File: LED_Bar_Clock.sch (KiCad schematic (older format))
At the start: 51 parts

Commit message: use core libraries for type c connector symbol
Some files seem to have changed format due to the change between
5.0.0 and 5.1.0 of KiCad. This is reflected in this commit
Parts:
- J?: symbol LED_Bar_Clock-rescue:USB_C_Receptacle_USB2.0-Connector -> Connector:USB_C_Receptacle_USB2.0
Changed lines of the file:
@@
 EESchema Schematic File Version 4
 LIBS:LED_Bar_Clock-cache
-EELAYER 26 0
+EELAYER 29 0
 EELAYER END
 $Descr A4 11693 8268
@@
 $EndComp
 $Comp
-L LED_Bar_Clock-rescue:USB_C_Receptacle_USB2.0-Connector J?
+L Connector:USB_C_Receptacle_USB2.0 J?
 U 1 1 5BF122DB
 P 3900 1150

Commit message: add annotations and power flags
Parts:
- gave numbers to parts that had none: 51
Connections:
- no-connect marks 2 -> 4

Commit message: change reset switch in schematic
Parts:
- removed SW1: SW_SPST, symbol Switch:SW_SPST
- added SW1: SKHMQKE010, Clock_Footprints:SKHMQKE010, symbol Clock_Symbols:SKHMQKE010
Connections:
- wire segments 191 -> 203
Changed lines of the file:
@@
 	3900 1950 4000 1950
-$Comp
-L Switch:SW_SPST SW1
-U 1 1 5CC780C2
-P 3850 4750
-F 0 "SW1" V 3804 4848 50  0000 L CNN
-F 1 "SW_SPST" V 3895 4848 50  0000 L CNN
-F 2 "" H 3850 4750 50  0001 C CNN
-F 3 "" H 3850 4750 50  0001 C CNN
-	1    3850 4750
-	0    1    1    0
-$EndComp
-$Comp
-L power:GND #PWR0120
-U 1 1 5CC781C6
-P 3850 5000
-F 0 "#PWR0120" H 3850 4750 50  0001 C CNN
-F 1 "GND" H 3855 4827 50  0000 C CNN
-F 2 "" H 3850 5000 50  0001 C CNN
-F 3 "" H 3850 5000 50  0001 C CNN
-	1    3850 5000
-	1    0    0    -1
-$EndComp
-Wire Wire Line
-	3850 5000 3850 4950
 $Comp
 L power:+5V #PWR0121
@@
 	3700 4500 3700 4550
 Connection ~ 3700 4550
-Wire Wire Line
-	3700 4550 3850 4550
 $Comp
 L Device:CP C3
@@
 	5100 1850 5100 1900
 Wire Wire Line
-	3850 4550 3950 4550
-Connection ~ 3850 4550
-Wire Wire Line
 	3950 4550 3950 4150
 Wire Wire Line
@@
 	1    0    0    -1
 $EndComp
+Wire Wire Line
+	3950 4750 3950 4700
+Wire Wire Line
+	3950 4700 3850 4700
+Wire Wire Line
+	3850 5200 3950 5200
+Wire Wire Line
+	3950 5200 3950 5150
+Wire Wire Line
+	4150 5150 4150 5200
+Wire Wire Line
+	4150 5200 4300 5200
+Wire Wire Line
+	4300 5200 4300 4700
+Wire Wire Line
+	4300 4700 4250 4700
+Wire Wire Line
+	4150 4700 4150 4750
+Wire Wire Line
+	4250 4750 4250 4700
+Connection ~ 4250 4700
+Wire Wire Line
+	4250 4700 4150 4700
+Wire Wire Line
+	3700 4550 3950 4550
+$Comp
+L Clock_Symbols:SKHMQKE010 SW1
+U 1 1 5CC7C44F
+P 4050 4950
+F 0 "SW1" H 4037 5275 50  0000 C CNN
+F 1 "SKHMQKE010" H 4037 5184 50  0000 C CNN
+F 2 "Clock_Footprints:SKHMQKE010" H 4050 5200 50  0001 C CNN
+F 3 "https://datasheet.lcsc.com/szlcsc/ALPS-Electric-SKHMQKE010_C202416.pdf" H 4050 5200 50  0001 C CNN
+	1    4050 4950
+	0    -1   -1   0
+$EndComp
+Wire Wire Line
+	3850 5200 3850 4700
+Wire Wire Line
+	3950 4700 3950 4550
+Connection ~ 3950 4700
+Connection ~ 3950 4550
+$Comp
+L power:GND #PWR01
+U 1 1 5CE4CD28
+P 4300 5300
+F 0 "#PWR01" H 4300 5050 50  0001 C CNN
+F 1 "GND" H 4305 5127 50  0000 C CNN
+F 2 "" H 4300 5300 50  0001 C CNN
+F 3 "" H 4300 5300 50  0001 C CNN
+	1    4300 5300
+	1    0    0    -1
+$EndComp
+Wire Wire Line
+	4300 5300 4300 5200
+Connection ~ 4300 5200
 $EndSCHEMATC

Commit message: Delete extra i2c junction
Hopefully I didn't break anything with the project component library
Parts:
- J1: symbol Connector:USB_C_Receptacle_USB2.0 -> LED_Bar_Clock-rescue:USB_C_Receptacle_USB2.0-Connector
- SW2: symbol Clock_Symbols:SW_5_Way -> LED_Bar_Clock-rescue:SW_5_Way-Clock_Symbols
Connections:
- wire segments 203 -> 202
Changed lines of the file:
@@
 EESchema Schematic File Version 4
 LIBS:LED_Bar_Clock-cache
-EELAYER 29 0
+EELAYER 26 0
 EELAYER END
 $Descr A4 11693 8268
@@
 $EndComp
 $Comp
-L Connector:USB_C_Receptacle_USB2.0 J1
+L LED_Bar_Clock-rescue:USB_C_Receptacle_USB2.0-Connector J1
 U 1 1 5BF122DB
 P 3900 1150
@@
 $EndComp
 $Comp
-L Clock_Symbols:SW_5_Way SW2
+L LED_Bar_Clock-rescue:SW_5_Way-Clock_Symbols SW2
 U 1 1 5CACD44D
 P 4350 2950
@@
 Wire Wire Line
 	2950 6250 2700 6250
-Wire Wire Line
-	2950 3950 4100 3950
 Wire Wire Line
 	3850 3750 3850 4050
@@
 	9900 6300 9900 5550
 Connection ~ 2850 3950
-Wire Wire Line
-	2850 3950 2950 3950
 Connection ~ 2950 3750
 Wire Wire Line
@@
 Wire Wire Line
 	2700 3950 2850 3950
-Wire Wire Line
-	2700 4050 3750 4050
 Wire Wire Line
 	2700 4250 3050 4250
@@
 	-1   0    0    1
 $EndComp
-Connection ~ 2950 3950
 Wire Wire Line
 	2950 3950 2950 6050
@@
 	4300 5300 4300 5200
 Connection ~ 4300 5200
+Wire Wire Line
+	2700 4050 3750 4050
+Wire Wire Line
+	2850 3950 4100 3950
 $EndSCHEMATC

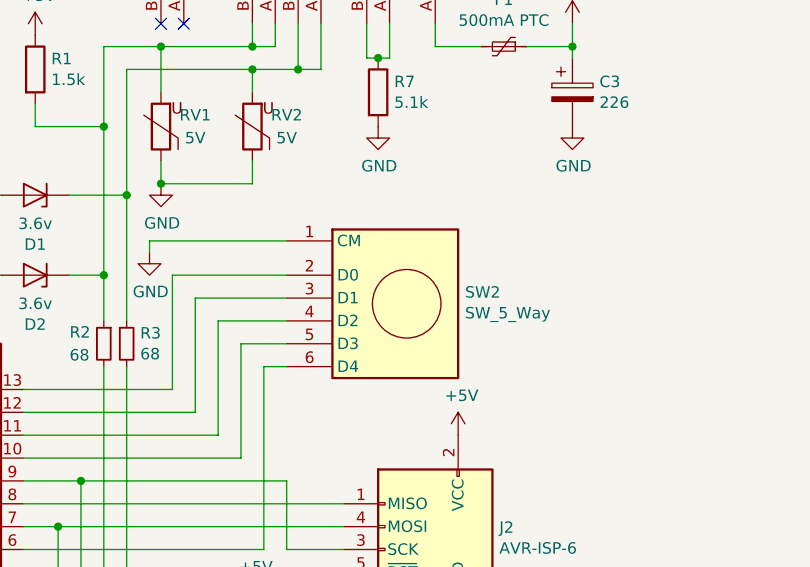
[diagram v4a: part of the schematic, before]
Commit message: Change duplicate pin 5 to pin 6 on 5-way switch
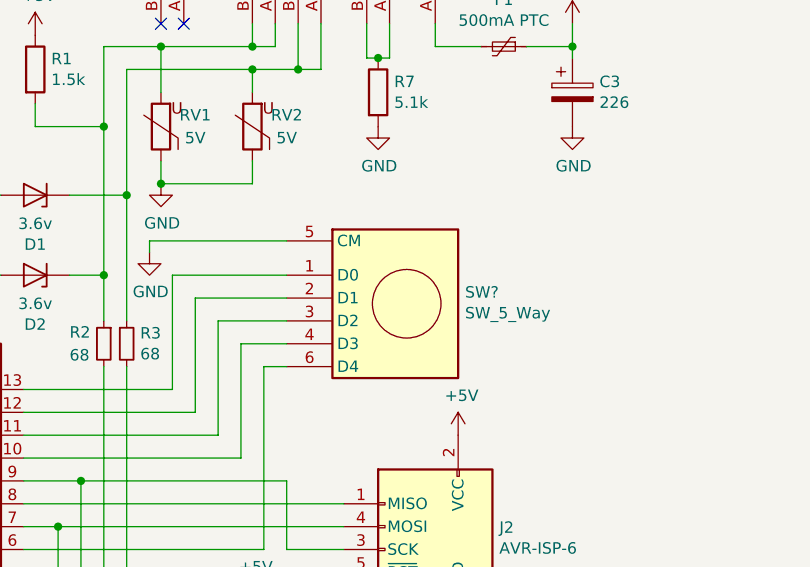
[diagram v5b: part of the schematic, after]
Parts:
- removed SW2: SW_5_Way, symbol LED_Bar_Clock-rescue:SW_5_Way-Clock_Symbols
- added SW?: SW_5_Way, symbol Clock_Symbols:SW_5_Way
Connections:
- net GND: now also SW?.5 (CM)
- net at U1.10 (PA3): now also SW?.4 (D3)
- net at U1.11 (PA2): now also SW?.3 (D2)
- net at U1.12 (PA1): now also SW?.2 (D1)
- net at U1.13 (AREF/PA0): now also SW?.1 (D0)
- net at U1.6 (PA7): now also SW?.6 (D4)
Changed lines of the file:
@@
 EESchema Schematic File Version 4
 LIBS:LED_Bar_Clock-cache
-EELAYER 26 0
+EELAYER 29 0
 EELAYER END
 $Descr A4 11693 8268
@@
 	1    0    0    -1
 $EndComp
-$Comp
-L LED_Bar_Clock-rescue:SW_5_Way-Clock_Symbols SW2
-U 1 1 5CACD44D
-P 4350 2950
-F 0 "SW2" H 4070 2975 50  0000 R CNN
-F 1 "SW_5_Way" H 4070 2884 50  0000 R CNN
-F 2 "" H 4325 2975 50  0001 C CNN
-F 3 "" H 4325 2975 50  0001 C CNN
-	1    4350 2950
-	-1   0    0    -1
-$EndComp
 Wire Wire Line
 	2850 6350 2700 6350
@@
 Wire Wire Line
 	2850 3950 4100 3950
+$Comp
+L Clock_Symbols:SW_5_Way SW?
+U 1 1 5CC8B05F
+P 4350 2950
+F 0 "SW?" H 4070 2975 50  0000 R CNN
+F 1 "SW_5_Way" H 4070 2884 50  0000 R CNN
+F 2 "" H 4325 2975 50  0001 C CNN
+F 3 "" H 4325 2975 50  0001 C CNN
+	1    4350 2950
+	-1   0    0    -1
+$EndComp
 $EndSCHEMATC

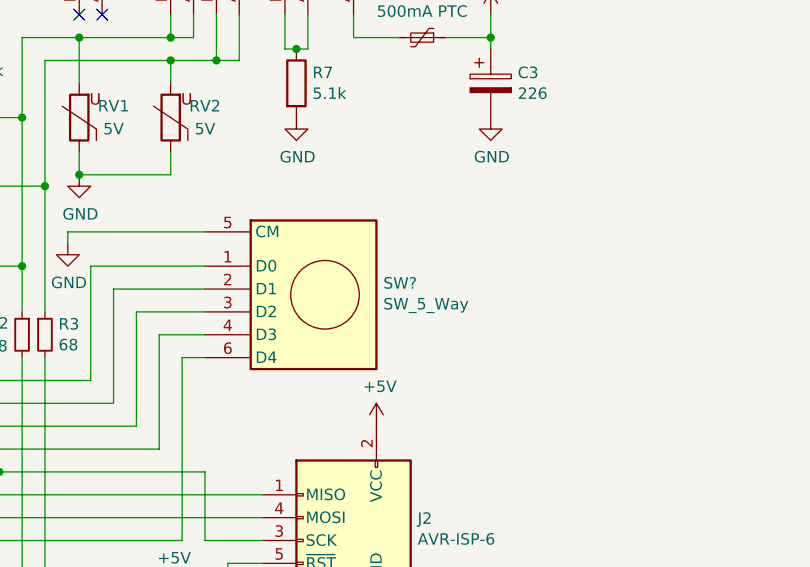
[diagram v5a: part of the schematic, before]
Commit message: assign footprints and create netlist
also remove netlist from .gitignore
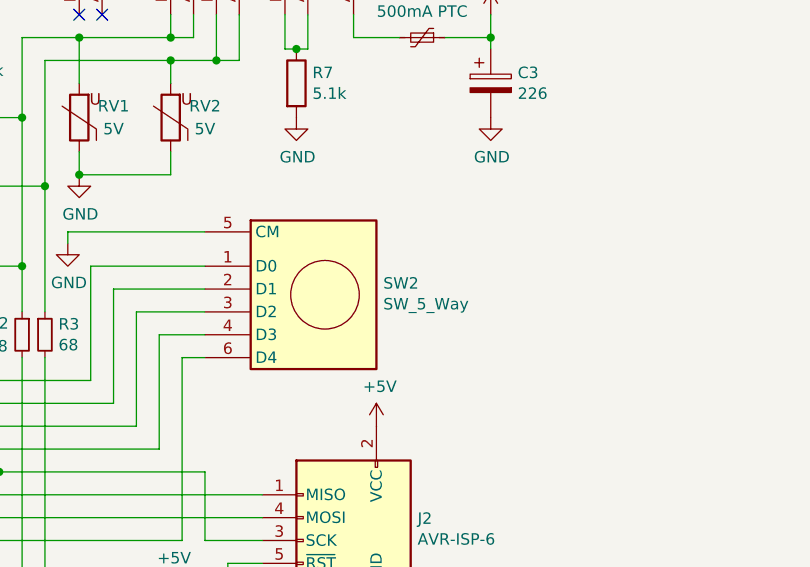
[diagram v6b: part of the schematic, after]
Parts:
- BT1: footprint (none) -> Clock_Footprints:BS-2-1
- C1, C10, C11, C12, C13, C14, C15, C16, C17, C2, C3, C4, C5, C6, C7, C8, C9: footprint (none) -> Capacitor_SMD:C_0603_1608Metric_Pad1.05x0.95mm_HandSolder
- D1, D2: footprint (none) -> Diode_SMD:D_SOD-123
- F1: footprint (none) -> Fuse:Fuse_0805_2012Metric
- J1: footprint (none) -> Clock_Footprints:U262-16XN-4BVC11
- J2: footprint (none) -> Connector_PinHeader_2.54mm:PinHeader_2x03_P2.54mm_Vertical
- R1, R2, R3, R4, R5, R6, R7, RV1, RV2: footprint (none) -> Resistor_SMD:R_0603_1608Metric_Pad1.05x0.95mm_HandSolder
- SW2: renamed from SW?; footprint (none) -> Clock_Footprints:K1-5203UA-01
- Y1: footprint (none) -> Crystal:Crystal_DS26_D2.0mm_L6.0mm_Horizontal
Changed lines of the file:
@@
 F 0 "J1" V 3959 1880 50  0000 L CNN
 F 1 "USB2.0 Type C Receptacle" V 4050 1880 50  0000 L CNN
-F 2 "" H 4050 1150 50  0001 C CNN
+F 2 "Clock_Footprints:U262-16XN-4BVC11" H 4050 1150 50  0001 C CNN
 F 3 "https://www.usb.org/sites/default/files/documents/usb_type-c.zip" H 4050 1150 50  0001 C CNN
 	1    3900 1150
@@
 F 0 "BT1" H 1218 6596 50  0000 L CNN
 F 1 "CR3032" H 1218 6505 50  0000 L CNN
-F 2 "" V 1100 6560 50  0001 C CNN
+F 2 "Clock_Footprints:BS-2-1" V 1100 6560 50  0001 C CNN
 F 3 "~" V 1100 6560 50  0001 C CNN
 	1    1100 6500
@@
 F 0 "C4" H 6742 1946 50  0000 L CNN
 F 1 "104" H 6742 1855 50  0000 L CNN
-F 2 "" H 6650 1900 50  0001 C CNN
+F 2 "Capacitor_SMD:C_0603_1608Metric_Pad1.05x0.95mm_HandSolder" H 6650 1900 50  0001 C CNN
 F 3 "~" H 6650 1900 50  0001 C CNN
 	1    6650 1900
@@
 F 0 "C5" H 6742 2746 50  0000 L CNN
 F 1 "104" H 6742 2655 50  0000 L CNN
-F 2 "" H 6650 2700 50  0001 C CNN
+F 2 "Capacitor_SMD:C_0603_1608Metric_Pad1.05x0.95mm_HandSolder" H 6650 2700 50  0001 C CNN
 F 3 "~" H 6650 2700 50  0001 C CNN
 	1    6650 2700
@@
 F 0 "C6" H 6742 3546 50  0000 L CNN
 F 1 "104" H 6742 3455 50  0000 L CNN
-F 2 "" H 6650 3500 50  0001 C CNN
+F 2 "Capacitor_SMD:C_0603_1608Metric_Pad1.05x0.95mm_HandSolder" H 6650 3500 50  0001 C CNN
 F 3 "~" H 6650 3500 50  0001 C CNN
 	1    6650 3500
@@
 F 0 "C7" H 6742 4346 50  0000 L CNN
 F 1 "104" H 6742 4255 50  0000 L CNN
-F 2 "" H 6650 4300 50  0001 C CNN
+F 2 "Capacitor_SMD:C_0603_1608Metric_Pad1.05x0.95mm_HandSolder" H 6650 4300 50  0001 C CNN
 F 3 "~" H 6650 4300 50  0001 C CNN
 	1    6650 4300
@@
 F 0 "C8" H 6742 5096 50  0000 L CNN
 F 1 "104" H 6742 5005 50  0000 L CNN
-F 2 "" H 6650 5050 50  0001 C CNN
+F 2 "Capacitor_SMD:C_0603_1608Metric_Pad1.05x0.95mm_HandSolder" H 6650 5050 50  0001 C CNN
 F 3 "~" H 6650 5050 50  0001 C CNN
 	1    6650 5050
@@
 F 0 "C9" H 6742 5846 50  0000 L CNN
 F 1 "104" H 6742 5755 50  0000 L CNN
-F 2 "" H 6650 5800 50  0001 C CNN
+F 2 "Capacitor_SMD:C_0603_1608Metric_Pad1.05x0.95mm_HandSolder" H 6650 5800 50  0001 C CNN
 F 3 "~" H 6650 5800 50  0001 C CNN
 	1    6650 5800
@@
 F 0 "C10" H 8042 3196 50  0000 L CNN
 F 1 "104" H 8042 3105 50  0000 L CNN
-F 2 "" H 7950 3150 50  0001 C CNN
+F 2 "Capacitor_SMD:C_0603_1608Metric_Pad1.05x0.95mm_HandSolder" H 7950 3150 50  0001 C CNN
 F 3 "~" H 7950 3150 50  0001 C CNN
 	1    7950 3150
@@
 F 0 "C11" H 8042 3996 50  0000 L CNN
 F 1 "104" H 8042 3905 50  0000 L CNN
-F 2 "" H 7950 3950 50  0001 C CNN
+F 2 "Capacitor_SMD:C_0603_1608Metric_Pad1.05x0.95mm_HandSolder" H 7950 3950 50  0001 C CNN
 F 3 "~" H 7950 3950 50  0001 C CNN
 	1    7950 3950
@@
 F 0 "C12" H 8042 4746 50  0000 L CNN
 F 1 "104" H 8042 4655 50  0000 L CNN
-F 2 "" H 7950 4700 50  0001 C CNN
+F 2 "Capacitor_SMD:C_0603_1608Metric_Pad1.05x0.95mm_HandSolder" H 7950 4700 50  0001 C CNN
 F 3 "~" H 7950 4700 50  0001 C CNN
 	1    7950 4700
@@
 F 0 "C13" H 9442 2396 50  0000 L CNN
 F 1 "104" H 9442 2305 50  0000 L CNN
-F 2 "" H 9350 2350 50  0001 C CNN
+F 2 "Capacitor_SMD:C_0603_1608Metric_Pad1.05x0.95mm_HandSolder" H 9350 2350 50  0001 C CNN
 F 3 "~" H 9350 2350 50  0001 C CNN
 	1    9350 2350
@@
 F 0 "C14" H 9442 3196 50  0000 L CNN
 F 1 "104" H 9442 3105 50  0000 L CNN
-F 2 "" H 9350 3150 50  0001 C CNN
+F 2 "Capacitor_SMD:C_0603_1608Metric_Pad1.05x0.95mm_HandSolder" H 9350 3150 50  0001 C CNN
 F 3 "~" H 9350 3150 50  0001 C CNN
 	1    9350 3150
@@
 F 0 "C15" H 9442 3996 50  0000 L CNN
 F 1 "104" H 9442 3905 50  0000 L CNN
-F 2 "" H 9350 3950 50  0001 C CNN
+F 2 "Capacitor_SMD:C_0603_1608Metric_Pad1.05x0.95mm_HandSolder" H 9350 3950 50  0001 C CNN
 F 3 "~" H 9350 3950 50  0001 C CNN
 	1    9350 3950
@@
 F 0 "C16" H 9442 4746 50  0000 L CNN
 F 1 "104" H 9442 4655 50  0000 L CNN
-F 2 "" H 9350 4700 50  0001 C CNN
+F 2 "Capacitor_SMD:C_0603_1608Metric_Pad1.05x0.95mm_HandSolder" H 9350 4700 50  0001 C CNN
 F 3 "~" H 9350 4700 50  0001 C CNN
 	1    9350 4700
@@
 F 0 "C17" H 9442 5496 50  0000 L CNN
 F 1 "104" H 9442 5405 50  0000 L CNN
-F 2 "" H 9350 5450 50  0001 C CNN
+F 2 "Capacitor_SMD:C_0603_1608Metric_Pad1.05x0.95mm_HandSolder" H 9350 5450 50  0001 C CNN
 F 3 "~" H 9350 5450 50  0001 C CNN
 	1    9350 5450
@@
 F 0 "Y1" V 3196 6619 50  0000 R CNN
 F 1 "32.768 kHz" V 3105 6619 50  0000 R CNN
-F 2 "" H 3150 6750 50  0001 C CNN
+F 2 "Crystal:Crystal_DS26_D2.0mm_L6.0mm_Horizontal" H 3150 6750 50  0001 C CNN
 F 3 "~" H 3150 6750 50  0001 C CNN
 	1    3150 6750
@@
 F 0 "J2" H 4220 4146 50  0000 R CNN
 F 1 "AVR-ISP-6" H 4220 4055 50  0000 R CNN
-F 2 "" V 4250 4100 50  0001 C CNN
+F 2 "Connector_PinHeader_2.54mm:PinHeader_2x03_P2.54mm_Vertical" V 4250 4100 50  0001 C CNN
 F 3 " ~" H 3225 3500 50  0001 C CNN
 	1    4500 4050
@@
 F 0 "R5" V 2943 6050 50  0000 C CNN
 F 1 "5.1k" V 3034 6050 50  0000 C CNN
-F 2 "" V 3080 6050 50  0001 C CNN
+F 2 "Resistor_SMD:R_0603_1608Metric_Pad1.05x0.95mm_HandSolder" V 3080 6050 50  0001 C CNN
 F 3 "~" H 3150 6050 50  0001 C CNN
 	1    3150 6050
@@
 F 0 "R4" V 2943 5550 50  0000 C CNN
 F 1 "5.1k" V 3034 5550 50  0000 C CNN
-F 2 "" V 3080 5550 50  0001 C CNN
+F 2 "Resistor_SMD:R_0603_1608Metric_Pad1.05x0.95mm_HandSolder" V 3080 5550 50  0001 C CNN
 F 3 "~" H 3150 5550 50  0001 C CNN
 	1    3150 5550
@@
 F 0 "R6" H 3759 4446 50  0000 L CNN
 F 1 "5.1k" H 3759 4355 50  0000 L CNN
-F 2 "" H 3700 4400 50  0001 C CNN
+F 2 "Resistor_SMD:R_0603_1608Metric_Pad1.05x0.95mm_HandSolder" H 3700 4400 50  0001 C CNN
 F 3 "~" H 3700 4400 50  0001 C CNN
 	1    3700 4400
@@
 F 0 "C3" H 5218 2096 50  0000 L CNN
 F 1 "226" H 5218 2005 50  0000 L CNN
-F 2 "" H 5138 1900 50  0001 C CNN
+F 2 "Capacitor_SMD:C_0603_1608Metric_Pad1.05x0.95mm_HandSolder" H 5138 1900 50  0001 C CNN
 F 3 "~" H 5100 2050 50  0001 C CNN
 	1    5100 2050
@@
 F 0 "C2" H 2542 5846 50  0000 L CNN
 F 1 "104" H 2542 5755 50  0000 L CNN
-F 2 "" H 2450 5800 50  0001 C CNN
+F 2 "Capacitor_SMD:C_0603_1608Metric_Pad1.05x0.95mm_HandSolder" H 2450 5800 50  0001 C CNN
 F 3 "~" H 2450 5800 50  0001 C CNN
 	1    2450 5800
@@
 F 0 "C1" H 1892 2846 50  0000 L CNN
 F 1 "104" H 1892 2755 50  0000 L CNN
-F 2 "" H 1800 2800 50  0001 C CNN
+F 2 "Capacitor_SMD:C_0603_1608Metric_Pad1.05x0.95mm_HandSolder" H 1800 2800 50  0001 C CNN
 F 3 "~" H 1800 2800 50  0001 C CNN
 	1    1800 2800
@@
 F 0 "R1" H 2820 1996 50  0000 L CNN
 F 1 "1.5k" H 2820 1905 50  0000 L CNN
-F 2 "" V 2680 1950 50  0001 C CNN
+F 2 "Resistor_SMD:R_0603_1608Metric_Pad1.05x0.95mm_HandSolder" V 2680 1950 50  0001 C CNN
 F 3 "~" H 2750 1950 50  0001 C CNN
 	1    2750 1950
@@
 F 0 "RV2" H 3550 2150 50  0000 C CNN
 F 1 "5V" H 3550 2250 50  0000 C CNN
-F 2 "" V 3630 2200 50  0001 C CNN
+F 2 "Resistor_SMD:R_0603_1608Metric_Pad1.05x0.95mm_HandSolder" V 3630 2200 50  0001 C CNN
 F 3 "~" H 3700 2200 50  0001 C CNN
 	1    3700 2200
@@
 F 0 "RV1" H 3150 2150 50  0000 C CNN
 F 1 "5V" H 3150 2250 50  0000 C CNN
-F 2 "" V 3230 2200 50  0001 C CNN
+F 2 "Resistor_SMD:R_0603_1608Metric_Pad1.05x0.95mm_HandSolder" V 3230 2200 50  0001 C CNN
 F 3 "~" H 3300 2200 50  0001 C CNN
 	1    3300 2200
@@
 F 0 "R7" H 4320 2096 50  0000 L CNN
 F 1 "5.1k" H 4320 2005 50  0000 L CNN
-F 2 "" V 4180 2050 50  0001 C CNN
+F 2 "Resistor_SMD:R_0603_1608Metric_Pad1.05x0.95mm_HandSolder" V 4180 2050 50  0001 C CNN
 F 3 "~" H 4250 2050 50  0001 C CNN
 	1    4250 2050
@@
 F 0 "D1" H 2750 2716 50  0000 C CNN
 F 1 "3.6v" H 2750 2625 50  0000 C CNN
-F 2 "" V 2750 2500 50  0001 C CNN
+F 2 "Diode_SMD:D_SOD-123" V 2750 2500 50  0001 C CNN
 F 3 "~" V 2750 2500 50  0001 C CNN
 	1    2750 2500
@@
 F 0 "F1" V 4595 1850 50  0000 C CNN
 F 1 "500mA PTC" V 4686 1850 50  0000 C CNN
-F 2 "" H 4850 1650 50  0001 L CNN
+F 2 "Fuse:Fuse_0805_2012Metric" H 4850 1650 50  0001 L CNN
 F 3 "~" H 4800 1850 50  0001 C CNN
 	1    4800 1850
@@
 F 0 "D2" H 2750 3066 50  0000 C CNN
 F 1 "3.6v" H 2750 2975 50  0000 C CNN
-F 2 "" V 2750 2850 50  0001 C CNN
+F 2 "Diode_SMD:D_SOD-123" V 2750 2850 50  0001 C CNN
 F 3 "~" V 2750 2850 50  0001 C CNN
 	1    2750 2850
@@
 F 0 "R3" H 3209 3196 50  0000 L CNN
 F 1 "68" H 3209 3105 50  0000 L CNN
-F 2 "" H 3150 3150 50  0001 C CNN
+F 2 "Resistor_SMD:R_0603_1608Metric_Pad1.05x0.95mm_HandSolder" H 3150 3150 50  0001 C CNN
 F 3 "~" H 3150 3150 50  0001 C CNN
 	1    3150 3150
@@
 F 0 "R2" H 3200 3200 50  0000 R CNN
 F 1 "68" H 3200 3100 50  0000 R CNN
-F 2 "" H 3050 3150 50  0001 C CNN
+F 2 "Resistor_SMD:R_0603_1608Metric_Pad1.05x0.95mm_HandSolder" H 3050 3150 50  0001 C CNN
 F 3 "~" H 3050 3150 50  0001 C CNN
 	1    3050 3150
@@
 	2850 3950 4100 3950
 $Comp
-L Clock_Symbols:SW_5_Way SW?
+L Clock_Symbols:SW_5_Way SW2
 U 1 1 5CC8B05F
 P 4350 2950
-F 0 "SW?" H 4070 2975 50  0000 R CNN
+F 0 "SW2" H 4070 2975 50  0000 R CNN
 F 1 "SW_5_Way" H 4070 2884 50  0000 R CNN
-F 2 "" H 4325 2975 50  0001 C CNN
+F 2 "Clock_Footprints:K1-5203UA-01" H 4325 2975 50  0001 C CNN
 F 3 "" H 4325 2975 50  0001 C CNN
 	1    4350 2950

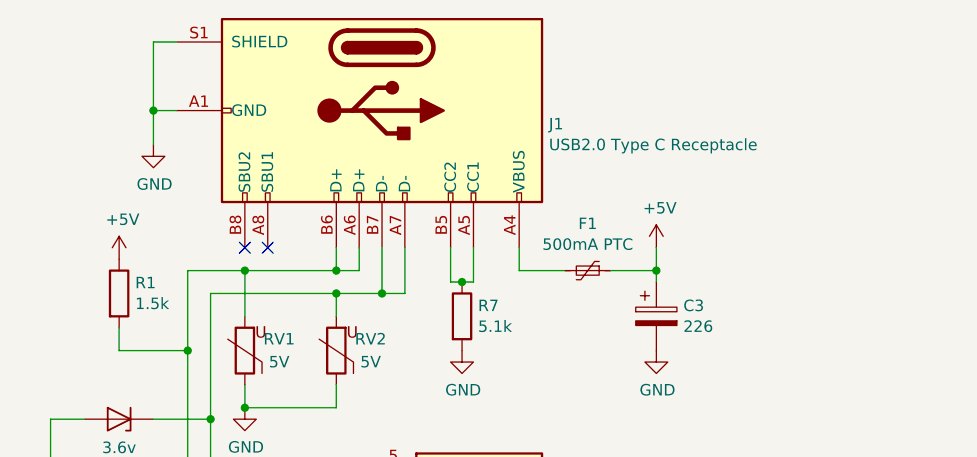
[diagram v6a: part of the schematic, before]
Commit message: Create custom symbol for usb receptacle
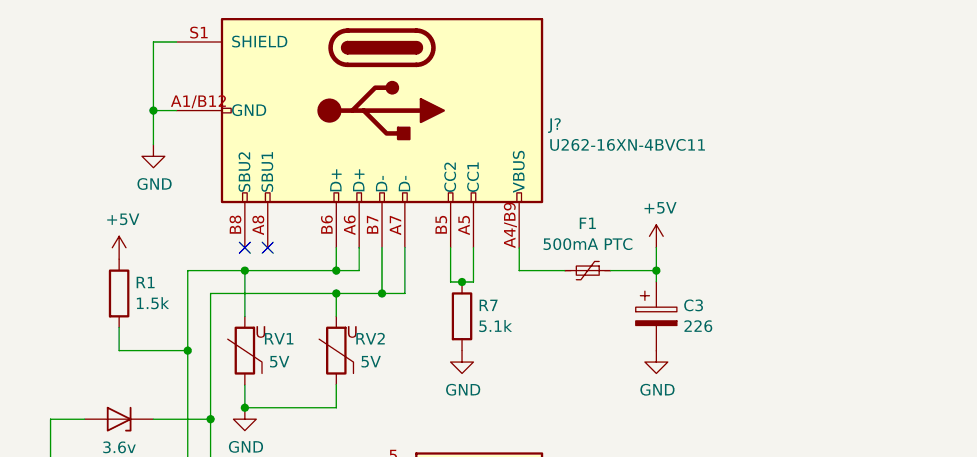
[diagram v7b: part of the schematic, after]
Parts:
- removed J1: USB2.0 Type C Receptacle, Clock_Footprints:U262-16XN-4BVC11, symbol LED_Bar_Clock-rescue:USB_C_Receptacle_USB2.0-Connector
- added J?: U262-16XN-4BVC11, Clock_Footprints:U262-16XN-4BVC11, symbol Clock_Symbols:U262-16XN-4BVC11
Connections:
- net GND: now also J?.A1/B12 (GND), J?.A12/B1 (GND), J?.S1 (SHIELD)
- net at F1.2: now also J?.A4/B9 (VBUS), J?.A9/B4 (VBUS)
- net at R7.1: now also J?.A5 (CC1), J?.B5 (CC2)
- net at D2.1 (K), R1.2, R2.1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: now also J?.A6 (D+), J?.B6 (D+)
- net at D1.1 (K), R3.1, RV2.2: now also J?.A7 (D-), J?.B7 (D-)
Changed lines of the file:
@@
 	0    -1   -1   0
-$EndComp
-$Comp
-L LED_Bar_Clock-rescue:USB_C_Receptacle_USB2.0-Connector J1
-U 1 1 5BF122DB
-P 3900 1150
-F 0 "J1" V 3959 1880 50  0000 L CNN
-F 1 "USB2.0 Type C Receptacle" V 4050 1880 50  0000 L CNN
-F 2 "Clock_Footprints:U262-16XN-4BVC11" H 4050 1150 50  0001 C CNN
-F 3 "https://www.usb.org/sites/default/files/documents/usb_type-c.zip" H 4050 1150 50  0001 C CNN
-	1    3900 1150
-	0    1    1    0
 $EndComp
 Text Notes 7320 7520 0    79   ~ 0
@@
 	-1   0    0    -1
 $EndComp
+$Comp
+L Clock_Symbols:U262-16XN-4BVC11 J?
+U 1 1 5CC92605
+P 3900 1150
+F 0 "J?" V 3961 1880 50  0000 L CNN
+F 1 "U262-16XN-4BVC11" V 4052 1880 50  0000 L CNN
+F 2 "Clock_Footprints:U262-16XN-4BVC11" H 4050 1150 50  0001 C CNN
+F 3 "https://www.usb.org/sites/default/files/documents/usb_type-c.zip" H 4050 1150 50  0001 C CNN
+	1    3900 1150
+	0    1    1    0
+$EndComp
 $EndSCHEMATC
